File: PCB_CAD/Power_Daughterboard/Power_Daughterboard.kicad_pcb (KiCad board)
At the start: 2 copper layers, 5 parts, among them J1 470531000, J2 CMF2.1111.12

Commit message: power daughterboard work
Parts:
- added PSU_bulk1: 100u, Capacitor_SMD:C_0805_2012Metric_Pad1.18x1.45mm_HandSolder, F.Cu at (169.0, 64.5)
- added PSU_noise1: 0.1u, Capacitor_SMD:C_0805_2012Metric_Pad1.18x1.45mm_HandSolder, F.Cu at (166.5, 53.0)
- moved PS1 108.5 mm to (133.0, 67.6), turned to 0 degrees
- moved J1 68.8 mm to (169.0, 68.0)
- moved J2 44.0 mm to (131.1, 84.8)
- moved RV1 41.6 mm to (120.5, 71.8), turned to 90 degrees
- moved F1 34.4 mm to (149.0, 75.0), turned to 180 degrees
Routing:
- net Net-(PS1-AC2): track 0.00 -> 42.0 mm
- net Net-(PS1-AC1): track 0.00 -> 32.3 mm
- net Net-(J2-Pad2): track 0.00 -> 20.0 mm
- net Net-(F1-Pad1): track 0.00 -> 18.6 mm
- net Net-(PS1-DC+): track 17.5 -> 29.8 mm
- net Net-(PS1-DC-): track 26.2 -> 24.5 mm
- added copper zone on F.Cu, net Net-(PS1-DC+)

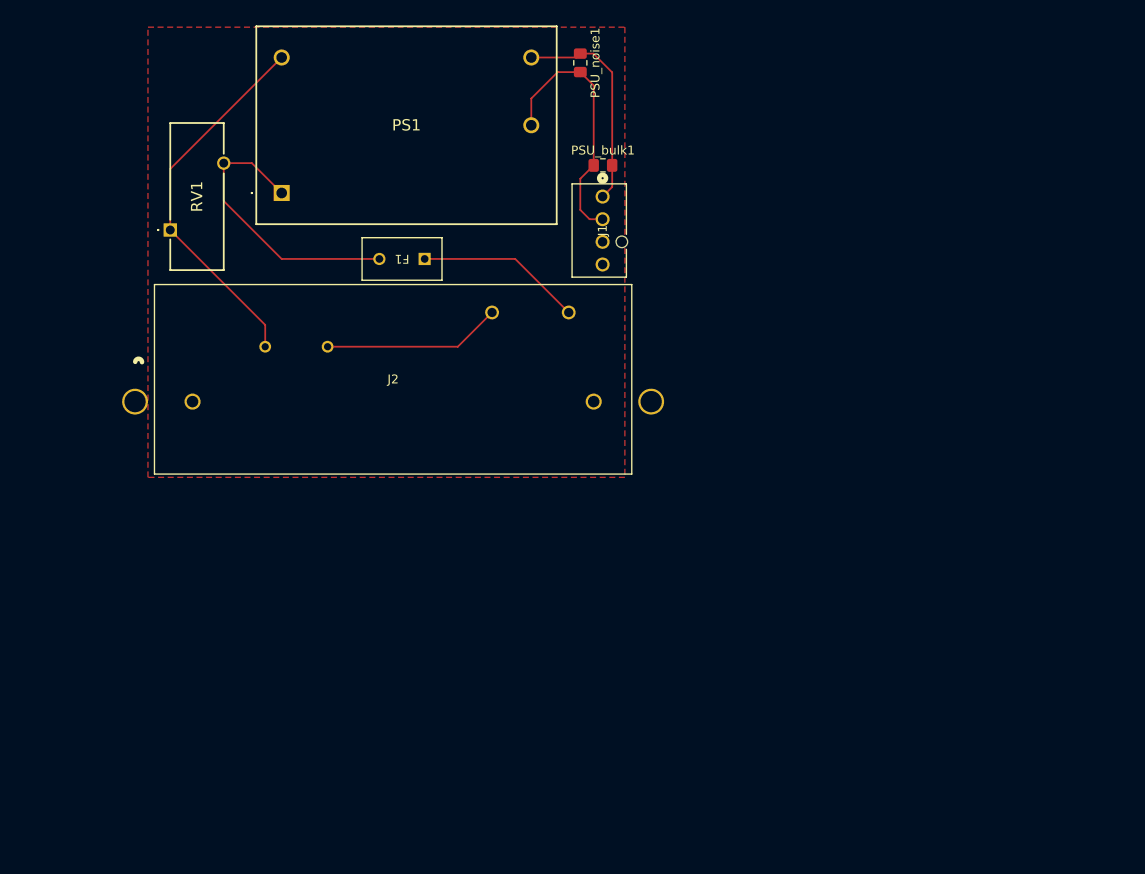
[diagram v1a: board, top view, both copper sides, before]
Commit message: work on power daughterboard
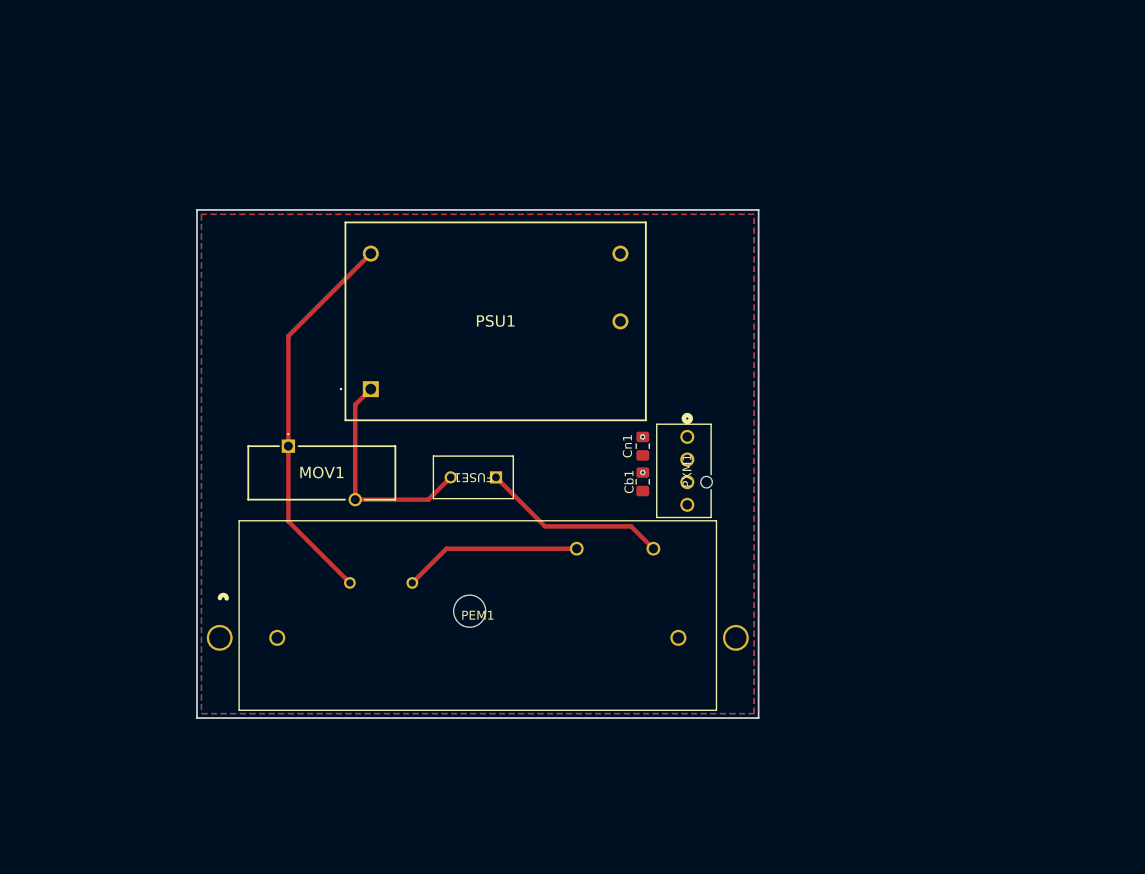
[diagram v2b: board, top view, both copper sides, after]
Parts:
- removed F1: SS-5H-1A-APH, CustomModels:FUSE_SS-5H-1A_EAT
- removed J1: 470531000, CustomModels:CONN_SD-47053-001_H10p00_MOL
- removed J2: CMF2.1111.12, CustomModels:CONN4_1131.12_SAI
- removed PS1: HP02S0300WI, CustomModels:HP02S0300WI
- removed PSU_bulk1: 100u, Capacitor_SMD:C_0805_2012Metric_Pad1.18x1.45mm_HandSolder
- removed PSU_noise1: 0.1u, Capacitor_SMD:C_0805_2012Metric_Pad1.18x1.45mm_HandSolder
- removed RV1: MOV-14D561KTR, CustomModels:MOV14D561KTR
- added Cb1: 100u, Capacitor_SMD:C_0805_2012Metric_Pad1.18x1.45mm_HandSolder, F.Cu at (173.5, 100.0)
- added Cn1: 0.1u, Capacitor_SMD:C_0805_2012Metric_Pad1.18x1.45mm_HandSolder, F.Cu at (173.5, 96.0)
- added FUSE1: SS-5H-1A-APH, CustomModels:FUSE_SS-5H-1A_EAT, F.Cu at (157.0, 99.5)
- added MOV1: MOV-14D561KTR, CustomModels:MOV14D561KTR, F.Cu at (133.8, 96.0)
- added PEM1: CMF2.1111.12, CustomModels:CONN4_1131.12_SAI, F.Cu at (140.6, 111.3)
- added PSU1: HP02S0300WI, CustomModels:HP02S0300WI, F.Cu at (143.0, 89.6)
- added PXM1: 470531000, CustomModels:CONN_SD-47053-001_H10p00_MOL, F.Cu at (178.5, 95.0)
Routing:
- net Net-(PSU1-AC2): track 0.00 -> 43.6 mm
- net Net-(PS1-AC2): track 42.0 -> 0.00 mm
- net Net-(PS1-AC1): track 32.3 -> 0.00 mm
- net Net-(PS1-DC+): track 29.8 -> 0.00 mm
- net Net-(PSU1-AC1): track 0.00 -> 24.9 mm
- net Net-(PS1-DC-): track 24.5 -> 0.00 mm
- net Net-(FUSE1-Pad1): track 0.00 -> 21.0 mm
- net Net-(PEM1-Pad2): track 0.00 -> 20.0 mm
- net Net-(J2-Pad2): track 20.0 -> 0.00 mm
- net Net-(F1-Pad1): track 18.6 -> 0.00 mm
- net /VOUT: vias 0 -> 2
- added copper zone on F.Cu, net /VGND
- added copper zone on B.Cu, net /VOUT
- removed copper zone on F.Cu, net Net-(PS1-DC+)
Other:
- board outline added: 63 x 57 mm

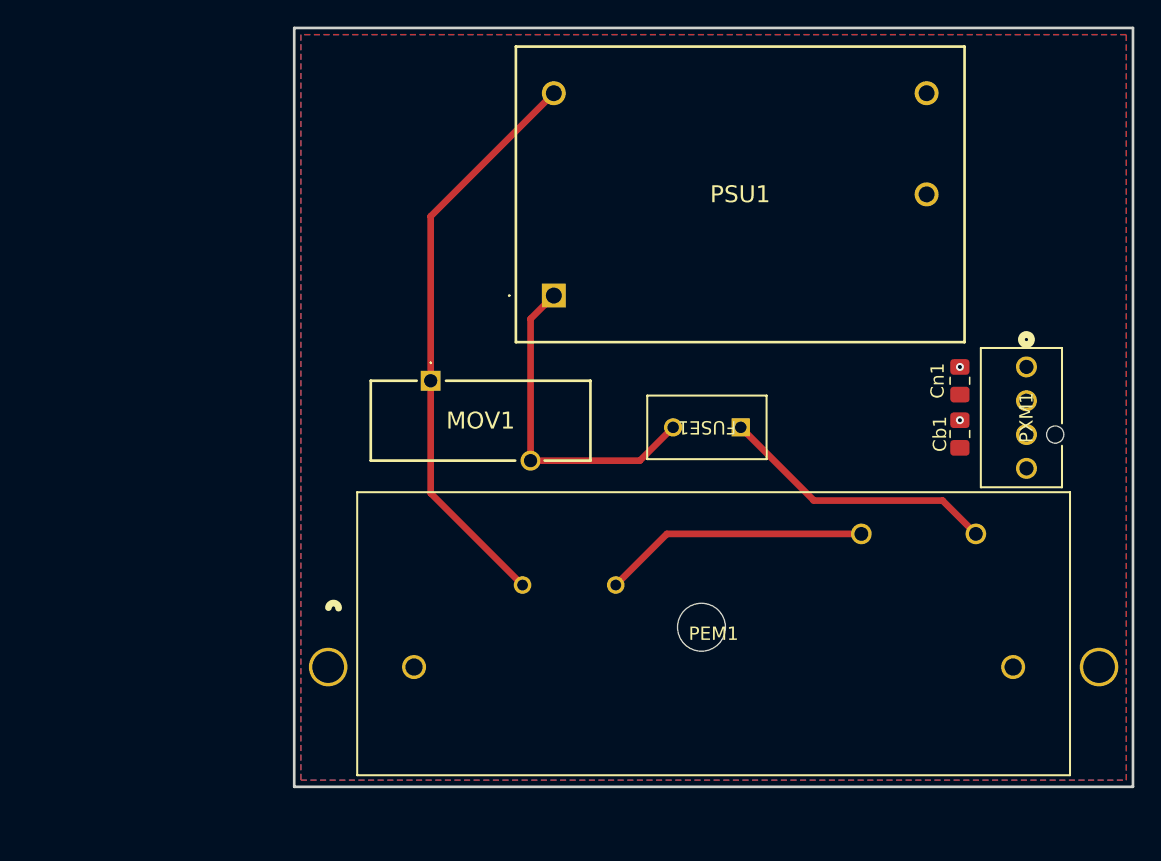
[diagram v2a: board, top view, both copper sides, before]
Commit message: power daughterboard finished
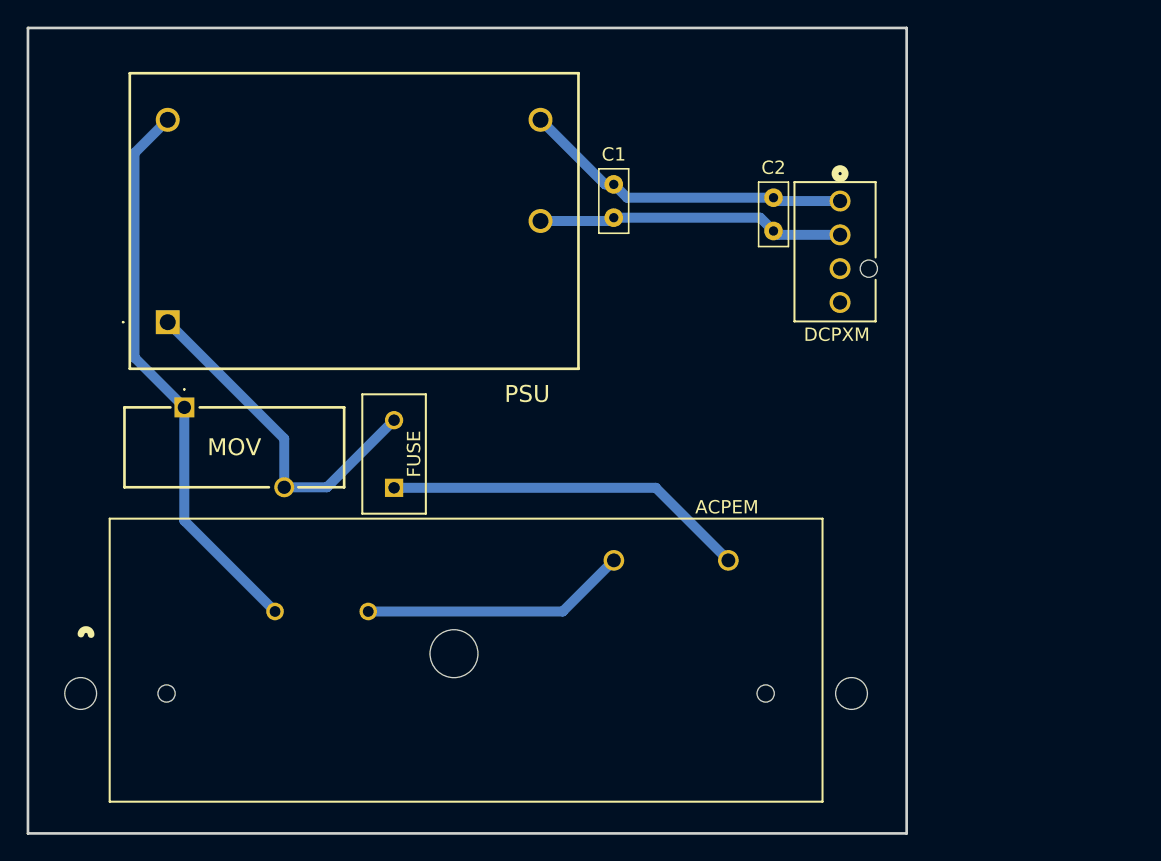
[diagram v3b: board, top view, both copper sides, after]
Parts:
- removed Cb1: 100u, Capacitor_SMD:C_0805_2012Metric_Pad1.18x1.45mm_HandSolder
- removed Cn1: 0.1u, Capacitor_SMD:C_0805_2012Metric_Pad1.18x1.45mm_HandSolder
- removed FUSE1: SS-5H-1A-APH, CustomModels:FUSE_SS-5H-1A_EAT
- removed MOV1: MOV-14D561KTR, CustomModels:MOV14D561KTR
- removed PEM1: CMF2.1111.12, CustomModels:CONN4_1131.12_SAI
- removed PSU1: HP02S0300WI, CustomModels:HP02S0300WI
- removed PXM1: 470531000, CustomModels:CONN_SD-47053-001_H10p00_MOL
- added ACPEM: CMF2.1111.12, CustomModels:CONN4_1131.12_SAI, F.Cu at (122.1, 113.3)
- added C1: 0.1u, Capacitor_THT:C_Rect_L4.6mm_W2.0mm_P2.50mm_MKS02_FKP02, F.Cu at (147.5, 83.8)
- added C2: 1u, Capacitor_THT:C_Rect_L4.6mm_W2.0mm_P2.50mm_MKS02_FKP02, F.Cu at (159.5, 84.8)
- added DCPXM: 470531000, CustomModels:CONN_SD-47053-001_H10p00_MOL, F.Cu at (164.5, 82.5)
- added FUSE: SS-5H-1A-APH, CustomModels:FUSE_SS-5H-1A_EAT, F.Cu at (131.0, 104.0)
- added MOV: MOV-14D561KTR, CustomModels:MOV14D561KTR, F.Cu at (115.2, 98.0)
- added PSU: HP02S0300WI, CustomModels:HP02S0300WI, F.Cu at (114.0, 91.6)
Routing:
- net Net-(PSU1-DC-): track 0.00 -> 25.0 mm
- net Net-(PSU1-DC+): track 0.00 -> 23.1 mm
- net Net-(FUSE1-Pad1): track 21.0 -> 27.4 mm
- net Net-(PSU1-AC1): track 24.9 -> 26.4 mm
- net Net-(PSU1-AC2): track 43.6 -> 42.3 mm
- net /VOUT: vias 2 -> 0
- removed copper zone on F.Cu, net /VGND
- removed copper zone on B.Cu, net /VOUT
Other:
- board size 63 x 57 mm -> 66 x 60.5 mm
- board text added: "C1"

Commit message: power daughterboard final review, some main schematic small fixes
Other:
- board text added: "AC 115~230V 50~60Hz IN DC 3.3V 600mA (2W) OUT Use a PC fan cable"
- board text added: "Liam Cringle CE Isaac Terrell EE Power daughterboard"
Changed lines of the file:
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@@
 		(layer "Edge.Cuts")
+	)
+	(gr_text "AC 115~230V 50~60Hz IN\nDC 3.3V 600mA (2W) OUT\nUse a PC fan cable"
+		(at 139.5 127.5 0)
+		(layer "B.SilkS")
+		(effects
+			(font
+				(size 1.5 1.5)
+				(thickness 0.3)
+				(bold yes)
+			)
+			(justify left bottom mirror)
+		)
+	)
+	(gr_text "Liam Cringle CE\nIsaac Terrell EE\nPower daughterboard"
+		(at 152.5 93.5 0)
+		(layer "B.SilkS")
+		(effects
+			(font
+				(size 1.5 1.5)
+				(thickness 0.3)
+				(bold yes)
+			)
+			(justify left bottom mirror)
+		)
 	)
 	(gr_text "C1"
@@
 	(segment
 		(start 129.060003 113.33)
-		(end 143.669998 113.33)
+		(end 132.900005 109.489998)
 		(width 0.75)
 		(layer "B.Cu")
@@
 	)
 	(segment
-		(start 143.669998 113.33)
+		(start 132.900005 109.489998)
 		(end 147.51 109.489998)
 		(width 0.75)

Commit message: Our long national nightmare is over
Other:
- board size 66 x 60.5 mm -> 65 x 60 mm
- board text added: "0.1µ"
- board text added: "1µ"
- board text removed: "C1"
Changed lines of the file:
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@@
 			(plot_on_all_layers_selection 0x0000000_00000000)
 			(disableapertmacros no)
-			(usegerberextensions no)
-			(usegerberattributes yes)
-			(usegerberadvancedattributes yes)
-			(creategerberjobfile yes)
+			(usegerberextensions yes)
+			(usegerberattributes no)
+			(usegerberadvancedattributes no)
+			(creategerberjobfile no)
 			(dashed_line_dash_ratio 12.000000)
 			(dashed_line_gap_ratio 3.000000)
@@
 			(psa4output no)
 			(plotreference yes)
-			(plotvalue yes)
+			(plotvalue no)
 			(plotfptext yes)
 			(plotinvisibletext no)
 			(sketchpadsonfab no)
-			(subtractmaskfromsilk no)
+			(subtractmaskfromsilk yes)
 			(outputformat 1)
 			(mirror no)
-			(drillshape 1)
+			(drillshape 0)
 			(scaleselection 1)
-			(outputdirectory "")
+			(outputdirectory "gerbers/")
 		)
 	)
@@
 			(at 4.75 0 180)
 			(layer "F.SilkS")
+			(hide yes)
 			(effects
 				(font
@@
 	)
 	(gr_rect
-		(start 103.5 69.5)
-		(end 169.5 130)
+		(start 104.5 69.5)
+		(end 169.5 129.5)
 		(stroke
 			(width 0.2)
@@
 		)
 	)
-	(gr_text "C1"
-		(at 147.5 79 0)
+	(gr_text "0.1µ"
+		(at 146.68 79.64 0)
 		(layer "F.SilkS")
 		(effects
@@
 				(thickness 0.15)
 			)
+			(justify left bottom)
 		)
 	)
+	(gr_text "1µ"
+		(at 158.13 80.43 0)
+		(layer "F.SilkS")
+		(effects
+			(font
+				(size 1 1)
+				(thickness 0.15)
+			)
+			(justify left bottom)
+		)
+	)
